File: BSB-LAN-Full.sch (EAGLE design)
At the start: 120 parts, among them IC1 LAN8710A-EZC, IC2 TPS2375D, IC3 TX4138, IC4 SY8089AAAC, IC6 CH340X, Q1 BC847, Q2 BC857, Q3 BC847, Q4 WPM2015-3/TR, Q5 BC847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

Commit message: Add CNMB/3 Footprint and Update Libs
Add footprint for the next size up enclosure.
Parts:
- OPT: device BSB-LAN:JUMPER-2PTH -> BSB-LAN:JUMPER-2-2MM
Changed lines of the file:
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@@
 <attribute name="LCSC_PART" value="C406156"/>
 </part>
-<part name="OPT" library="BSB-LAN" deviceset="JUMPER-2" device="PTH" value="DNI"/>
+<part name="OPT" library="BSB-LAN" deviceset="JUMPER-2" device="-2MM" value="DNI"/>
 <part name="Q5" library="BSB-LAN" deviceset="BC847*" device="" value="BC847">
 <attribute name="LCSC_PART" value="C130417"/>

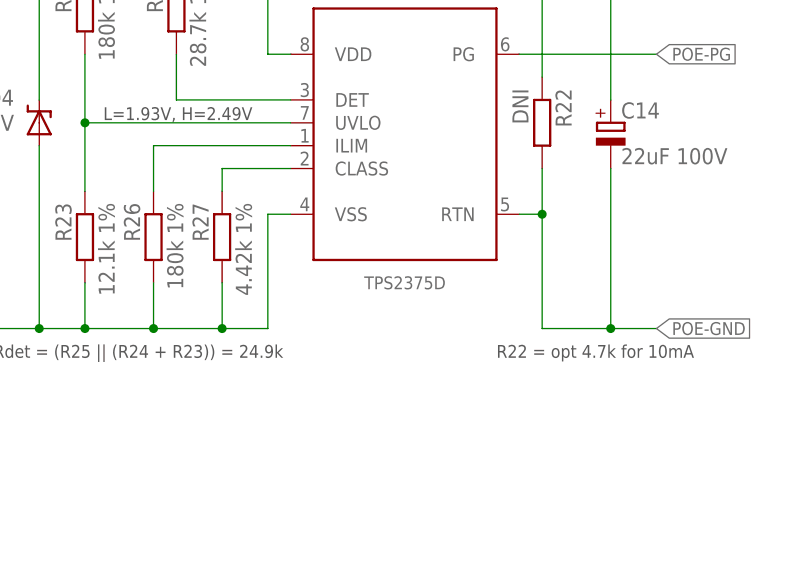
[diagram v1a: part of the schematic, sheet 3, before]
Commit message: Correct PoE IC Part Number
The LCSC_PART selected was the TPS2376DDA but the schematic value was TPS2375D, This actually has a slightly different footprint - the DDA has a thermal pad.

Update to account for the change.
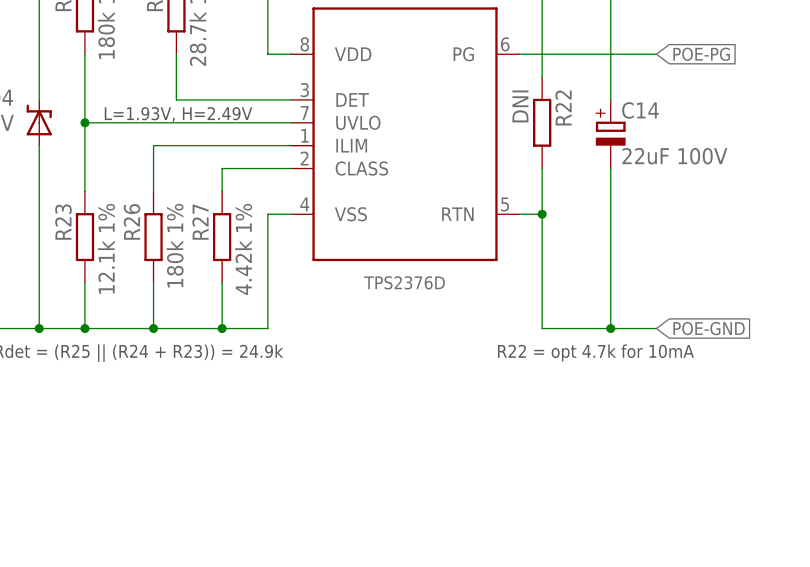
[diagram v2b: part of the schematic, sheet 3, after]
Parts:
- IC2: value TPS2375D -> TPS2376D; device BSB-LAN:TPS2375D -> BSB-LAN:TPS2376D
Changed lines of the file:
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@@
 <grid distance="0.1" unitdist="inch" unit="inch" style="lines" multiple="1" display="no" altdistance="0.01" altunitdist="inch" altunit="inch"/>
 <layers>
-<layer number="1" name="Top" color="4" fill="1" visible="no" active="no"/>
-<layer number="2" name="Route2" color="1" fill="3" visible="no" active="no"/>
-<layer number="3" name="Route3" color="4" fill="3" visible="no" active="no"/>
-<layer number="4" name="Route4" color="1" fill="4" visible="no" active="no"/>
-<layer number="5" name="Route5" color="4" fill="4" visible="no" active="no"/>
-<layer number="6" name="Route6" color="1" fill="8" visible="no" active="no"/>
-<layer number="7" name="Route7" color="4" fill="8" visible="no" active="no"/>
-<layer number="8" name="Route8" color="1" fill="2" visible="no" active="no"/>
-<layer number="9" name="Route9" color="4" fill="2" visible="no" active="no"/>
-<layer number="10" name="Route10" color="1" fill="7" visible="no" active="no"/>
-<layer number="11" name="Route11" color="4" fill="7" visible="no" active="no"/>
-<layer number="12" name="Route12" color="1" fill="5" visible="no" active="no"/>
-<layer number="13" name="Route13" color="4" fill="5" visible="no" active="no"/>
-<layer number="14" name="Route14" color="1" fill="6" visible="no" active="no"/>
-<layer number="15" name="Route15" color="4" fill="6" visible="no" active="no"/>
-<layer number="16" name="Bottom" color="1" fill="1" visible="no" active="no"/>
-<layer number="17" name="Pads" color="2" fill="1" visible="no" active="no"/>
-<layer number="18" name="Vias" color="2" fill="1" visible="no" active="no"/>
-<layer number="19" name="Unrouted" color="6" fill="1" visible="no" active="no"/>
-<layer number="20" name="Dimension" color="15" fill="1" visible="no" active="no"/>
-<layer number="21" name="tPlace" color="7" fill="1" visible="no" active="no"/>
-<layer number="22" name="bPlace" color="7" fill="1" visible="no" active="no"/>
-<layer number="23" name="tOrigins" color="15" fill="1" visible="no" active="no"/>
-<layer number="24" name="bOrigins" color="15" fill="1" visible="no" active="no"/>
-<layer number="25" name="tNames" color="7" fill="1" visible="no" active="no"/>
-<layer number="26" name="bNames" color="7" fill="1" visible="no" active="no"/>
-<layer number="27" name="tValues" color="7" fill="1" visible="no" active="no"/>
-<layer number="28" name="bValues" color="7" fill="1" visible="no" active="no"/>
+<layer number="1" name="Top" color="4" fill="1" visible="yes" active="no"/>
+<layer number="2" name="Route2" color="1" fill="3" visible="yes" active="no"/>
+<layer number="3" name="Route3" color="4" fill="3" visible="yes" active="no"/>
+<layer number="4" name="Route4" color="1" fill="4" visible="yes" active="no"/>
+<layer number="5" name="Route5" color="4" fill="4" visible="yes" active="no"/>
+<layer number="6" name="Route6" color="1" fill="8" visible="yes" active="no"/>
+<layer number="7" name="Route7" color="4" fill="8" visible="yes" active="no"/>
+<layer number="8" name="Route8" color="1" fill="2" visible="yes" active="no"/>
+<layer number="9" name="Route9" color="4" fill="2" visible="yes" active="no"/>
+<layer number="10" name="Route10" color="1" fill="7" visible="yes" active="no"/>
+<layer number="11" name="Route11" color="4" fill="7" visible="yes" active="no"/>
+<layer number="12" name="Route12" color="1" fill="5" visible="yes" active="no"/>
+<layer number="13" name="Route13" color="4" fill="5" visible="yes" active="no"/>
+<layer number="14" name="Route14" color="1" fill="6" visible="yes" active="no"/>
+<layer number="15" name="Route15" color="4" fill="6" visible="yes" active="no"/>
+<layer number="16" name="Bottom" color="1" fill="1" visible="yes" active="no"/>
+<layer number="17" name="Pads" color="2" fill="1" visible="yes" active="no"/>
+<layer number="18" name="Vias" color="2" fill="1" visible="yes" active="no"/>
+<layer number="19" name="Unrouted" color="6" fill="1" visible="yes" active="no"/>
+<layer number="20" name="Dimension" color="15" fill="1" visible="yes" active="no"/>
+<layer number="21" name="tPlace" color="7" fill="1" visible="yes" active="no"/>
+<layer number="22" name="bPlace" color="7" fill="1" visible="yes" active="no"/>
+<layer number="23" name="tOrigins" color="15" fill="1" visible="yes" active="no"/>
+<layer number="24" name="bOrigins" color="15" fill="1" visible="yes" active="no"/>
+<layer number="25" name="tNames" color="7" fill="1" visible="yes" active="no"/>
+<layer number="26" name="bNames" color="7" fill="1" visible="yes" active="no"/>
+<layer number="27" name="tValues" color="7" fill="1" visible="yes" active="no"/>
+<layer number="28" name="bValues" color="7" fill="1" visible="yes" active="no"/>
 <layer number="29" name="tStop" color="7" fill="3" visible="no" active="no"/>
 <layer number="30" name="bStop" color="7" fill="6" visible="no" active="no"/>
@@
 <layer number="35" name="tGlue" color="7" fill="4" visible="no" active="no"/>
 <layer number="36" name="bGlue" color="7" fill="5" visible="no" active="no"/>
-<layer number="37" name="tTest" color="7" fill="1" visible="no" active="no"/>
-<layer number="38" name="bTest" color="7" fill="1" visible="no" active="no"/>
+<layer number="37" name="tTest" color="7" fill="1" visible="yes" active="no"/>
+<layer number="38" name="bTest" color="7" fill="1" visible="yes" active="no"/>
 <layer number="39" name="tKeepout" color="4" fill="11" visible="no" active="no"/>
 <layer number="40" name="bKeepout" color="1" fill="11" visible="no" active="no"/>
@@
 <layer number="44" name="Drills" color="7" fill="1" visible="no" active="no"/>
 <layer number="45" name="Holes" color="7" fill="1" visible="no" active="no"/>
-<layer number="46" name="Milling" color="3" fill="1" visible="no" active="no"/>
-<layer number="47" name="Measures" color="7" fill="1" visible="no" active="no"/>
-<layer number="48" name="Document" color="7" fill="1" visible="no" active="no"/>
-<layer number="49" name="Reference" color="7" fill="1" visible="no" active="no"/>
-<layer number="50" name="dxf" color="7" fill="1" visible="no" active="no"/>
-<layer number="51" name="tDocu" color="7" fill="1" visible="no" active="no"/>
-<layer number="52" name="bDocu" color="7" fill="1" visible="no" active="no"/>
-<layer number="53" name="tGND_GNDA" color="7" fill="9" visible="no" active="no"/>
-<layer number="54" name="bGND_GNDA" color="1" fill="9" visible="no" active="no"/>
-<layer number="56" name="wert" color="7" fill="1" visible="no" active="no"/>
-<layer number="57" name="tCAD" color="7" fill="1" visible="no" active="no"/>
-<layer number="58" name="bCAD" color="7" fill="1" visible="no" active="no"/>
-<layer number="59" name="tCarbon" color="7" fill="1" visible="no" active="no"/>
-<layer number="60" name="bCarbon" color="7" fill="1" visible="no" active="no"/>
+<layer number="46" name="Milling" color="3" fill="1" visible="yes" active="no"/>
+<layer number="47" name="Measures" color="7" fill="1" visible="yes" active="no"/>
+<layer number="48" name="Document" color="7" fill="1" visible="yes" active="no"/>
+<layer number="49" name="Reference" color="7" fill="1" visible="yes" active="no"/>
+<layer number="50" name="dxf" color="7" fill="1" visible="yes" active="no"/>
+<layer number="51" name="tDocu" color="7" fill="1" visible="yes" active="no"/>
+<layer number="52" name="bDocu" color="7" fill="1" visible="yes" active="no"/>
+<layer number="53" name="tGND_GNDA" color="7" fill="9" visible="yes" active="no"/>
+<layer number="54" name="bGND_GNDA" color="1" fill="9" visible="yes" active="no"/>
+<layer number="56" name="wert" color="7" fill="1" visible="yes" active="no"/>
+<layer number="57" name="tCAD" color="7" fill="1" visible="yes" active="no"/>
+<layer number="58" name="bCAD" color="7" fill="1" visible="yes" active="no"/>
+<layer number="59" name="tCarbon" color="7" fill="1" visible="yes" active="no"/>
+<layer number="60" name="bCarbon" color="7" fill="1" visible="yes" active="no"/>
 <layer number="88" name="SimResults" color="9" fill="1" visible="yes" active="yes"/>
 <layer number="89" name="SimProbes" color="9" fill="1" visible="yes" active="yes"/>
@@
 <attribute name="LCSC_PART" value="C113803"/>
 </part>
-<part name="IC2" library="BSB-LAN" deviceset="TPS2375" device="D"/>
+<part name="IC2" library="BSB-LAN" deviceset="TPS237*" device="D" technology="6"/>
 <part name="D4" library="BSB-LAN" deviceset="TVS-UNI" device="SMA" value="58V">
 <attribute name="LCSC_PART" value="C151246"/>

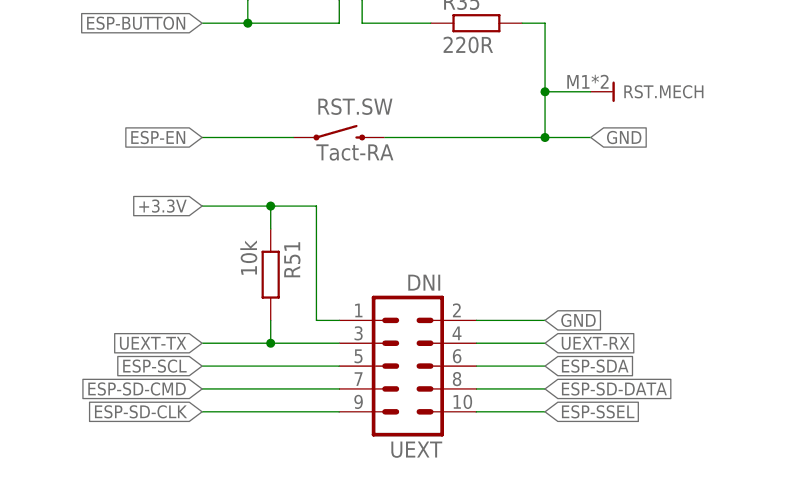
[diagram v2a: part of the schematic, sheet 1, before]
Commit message: Correct Component Rotation Values in JLC CPL
Add rotation correction factors to parts which import in the wrong orientation.
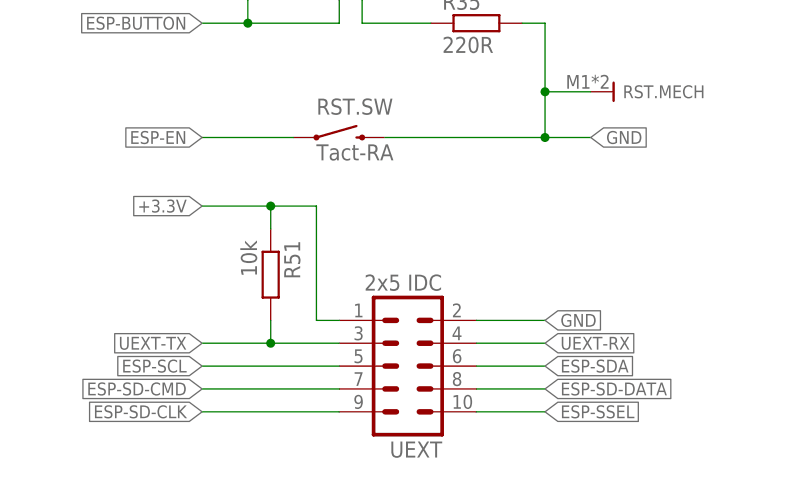
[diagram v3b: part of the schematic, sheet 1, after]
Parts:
- UEXT: value DNI -> 2x5 IDC
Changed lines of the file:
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@@
 <grid distance="0.1" unitdist="inch" unit="inch" style="lines" multiple="1" display="no" altdistance="0.01" altunitdist="inch" altunit="inch"/>
 <layers>
-<layer number="1" name="Top" color="4" fill="1" visible="yes" active="no"/>
-<layer number="2" name="Route2" color="1" fill="3" visible="yes" active="no"/>
-<layer number="3" name="Route3" color="4" fill="3" visible="yes" active="no"/>
-<layer number="4" name="Route4" color="1" fill="4" visible="yes" active="no"/>
-<layer number="5" name="Route5" color="4" fill="4" visible="yes" active="no"/>
-<layer number="6" name="Route6" color="1" fill="8" visible="yes" active="no"/>
-<layer number="7" name="Route7" color="4" fill="8" visible="yes" active="no"/>
-<layer number="8" name="Route8" color="1" fill="2" visible="yes" active="no"/>
-<layer number="9" name="Route9" color="4" fill="2" visible="yes" active="no"/>
-<layer number="10" name="Route10" color="1" fill="7" visible="yes" active="no"/>
-<layer number="11" name="Route11" color="4" fill="7" visible="yes" active="no"/>
-<layer number="12" name="Route12" color="1" fill="5" visible="yes" active="no"/>
-<layer number="13" name="Route13" color="4" fill="5" visible="yes" active="no"/>
-<layer number="14" name="Route14" color="1" fill="6" visible="yes" active="no"/>
-<layer number="15" name="Route15" color="4" fill="6" visible="yes" active="no"/>
-<layer number="16" name="Bottom" color="1" fill="1" visible="yes" active="no"/>
-<layer number="17" name="Pads" color="2" fill="1" visible="yes" active="no"/>
-<layer number="18" name="Vias" color="2" fill="1" visible="yes" active="no"/>
-<layer number="19" name="Unrouted" color="6" fill="1" visible="yes" active="no"/>
-<layer number="20" name="Dimension" color="15" fill="1" visible="yes" active="no"/>
-<layer number="21" name="tPlace" color="7" fill="1" visible="yes" active="no"/>
-<layer number="22" name="bPlace" color="7" fill="1" visible="yes" active="no"/>
-<layer number="23" name="tOrigins" color="15" fill="1" visible="yes" active="no"/>
-<layer number="24" name="bOrigins" color="15" fill="1" visible="yes" active="no"/>
-<layer number="25" name="tNames" color="7" fill="1" visible="yes" active="no"/>
-<layer number="26" name="bNames" color="7" fill="1" visible="yes" active="no"/>
-<layer number="27" name="tValues" color="7" fill="1" visible="yes" active="no"/>
-<layer number="28" name="bValues" color="7" fill="1" visible="yes" active="no"/>
+<layer number="1" name="Top" color="4" fill="1" visible="no" active="no"/>
+<layer number="2" name="Route2" color="1" fill="3" visible="no" active="no"/>
+<layer number="3" name="Route3" color="4" fill="3" visible="no" active="no"/>
+<layer number="4" name="Route4" color="1" fill="4" visible="no" active="no"/>
+<layer number="5" name="Route5" color="4" fill="4" visible="no" active="no"/>
+<layer number="6" name="Route6" color="1" fill="8" visible="no" active="no"/>
+<layer number="7" name="Route7" color="4" fill="8" visible="no" active="no"/>
+<layer number="8" name="Route8" color="1" fill="2" visible="no" active="no"/>
+<layer number="9" name="Route9" color="4" fill="2" visible="no" active="no"/>
+<layer number="10" name="Route10" color="1" fill="7" visible="no" active="no"/>
+<layer number="11" name="Route11" color="4" fill="7" visible="no" active="no"/>
+<layer number="12" name="Route12" color="1" fill="5" visible="no" active="no"/>
+<layer number="13" name="Route13" color="4" fill="5" visible="no" active="no"/>
+<layer number="14" name="Route14" color="1" fill="6" visible="no" active="no"/>
+<layer number="15" name="Route15" color="4" fill="6" visible="no" active="no"/>
+<layer number="16" name="Bottom" color="1" fill="1" visible="no" active="no"/>
+<layer number="17" name="Pads" color="2" fill="1" visible="no" active="no"/>
+<layer number="18" name="Vias" color="2" fill="1" visible="no" active="no"/>
+<layer number="19" name="Unrouted" color="6" fill="1" visible="no" active="no"/>
+<layer number="20" name="Dimension" color="15" fill="1" visible="no" active="no"/>
+<layer number="21" name="tPlace" color="7" fill="1" visible="no" active="no"/>
+<layer number="22" name="bPlace" color="7" fill="1" visible="no" active="no"/>
+<layer number="23" name="tOrigins" color="15" fill="1" visible="no" active="no"/>
+<layer number="24" name="bOrigins" color="15" fill="1" visible="no" active="no"/>
+<layer number="25" name="tNames" color="7" fill="1" visible="no" active="no"/>
+<layer number="26" name="bNames" color="7" fill="1" visible="no" active="no"/>
+<layer number="27" name="tValues" color="7" fill="1" visible="no" active="no"/>
+<layer number="28" name="bValues" color="7" fill="1" visible="no" active="no"/>
 <layer number="29" name="tStop" color="7" fill="3" visible="no" active="no"/>
 <layer number="30" name="bStop" color="7" fill="6" visible="no" active="no"/>
@@
 <layer number="35" name="tGlue" color="7" fill="4" visible="no" active="no"/>
 <layer number="36" name="bGlue" color="7" fill="5" visible="no" active="no"/>
-<layer number="37" name="tTest" color="7" fill="1" visible="yes" active="no"/>
-<layer number="38" name="bTest" color="7" fill="1" visible="yes" active="no"/>
+<layer number="37" name="tTest" color="7" fill="1" visible="no" active="no"/>
+<layer number="38" name="bTest" color="7" fill="1" visible="no" active="no"/>
 <layer number="39" name="tKeepout" color="4" fill="11" visible="no" active="no"/>
 <layer number="40" name="bKeepout" color="1" fill="11" visible="no" active="no"/>
@@
 <layer number="44" name="Drills" color="7" fill="1" visible="no" active="no"/>
 <layer number="45" name="Holes" color="7" fill="1" visible="no" active="no"/>
-<layer number="46" name="Milling" color="3" fill="1" visible="yes" active="no"/>
-<layer number="47" name="Measures" color="7" fill="1" visible="yes" active="no"/>
-<layer number="48" name="Document" color="7" fill="1" visible="yes" active="no"/>
-<layer number="49" name="Reference" color="7" fill="1" visible="yes" active="no"/>
-<layer number="50" name="dxf" color="7" fill="1" visible="yes" active="no"/>
-<layer number="51" name="tDocu" color="7" fill="1" visible="yes" active="no"/>
-<layer number="52" name="bDocu" color="7" fill="1" visible="yes" active="no"/>
-<layer number="53" name="tGND_GNDA" color="7" fill="9" visible="yes" active="no"/>
-<layer number="54" name="bGND_GNDA" color="1" fill="9" visible="yes" active="no"/>
-<layer number="56" name="wert" color="7" fill="1" visible="yes" active="no"/>
-<layer number="57" name="tCAD" color="7" fill="1" visible="yes" active="no"/>
-<layer number="58" name="bCAD" color="7" fill="1" visible="yes" active="no"/>
-<layer number="59" name="tCarbon" color="7" fill="1" visible="yes" active="no"/>
-<layer number="60" name="bCarbon" color="7" fill="1" visible="yes" active="no"/>
+<layer number="46" name="Milling" color="3" fill="1" visible="no" active="no"/>
+<layer number="47" name="Measures" color="7" fill="1" visible="no" active="no"/>
+<layer number="48" name="Document" color="7" fill="1" visible="no" active="no"/>
+<layer number="49" name="Reference" color="7" fill="1" visible="no" active="no"/>
+<layer number="50" name="dxf" color="7" fill="1" visible="no" active="no"/>
+<layer number="51" name="tDocu" color="7" fill="1" visible="no" active="no"/>
+<layer number="52" name="bDocu" color="7" fill="1" visible="no" active="no"/>
+<layer number="53" name="tGND_GNDA" color="7" fill="9" visible="no" active="no"/>
+<layer number="54" name="bGND_GNDA" color="1" fill="9" visible="no" active="no"/>
+<layer number="56" name="wert" color="7" fill="1" visible="no" active="no"/>
+<layer number="57" name="tCAD" color="7" fill="1" visible="no" active="no"/>
+<layer number="58" name="bCAD" color="7" fill="1" visible="no" active="no"/>
+<layer number="59" name="tCarbon" color="7" fill="1" visible="no" active="no"/>
+<layer number="60" name="bCarbon" color="7" fill="1" visible="no" active="no"/>
 <layer number="88" name="SimResults" color="9" fill="1" visible="yes" active="yes"/>
 <layer number="89" name="SimProbes" color="9" fill="1" visible="yes" active="yes"/>
@@
 <attribute name="LCSC_PART" value="C426782"/>
 </part>
-<part name="UEXT" library="BSB-LAN" deviceset="ML10" device="" value="DNI"/>
+<part name="UEXT" library="BSB-LAN" deviceset="ML10" device="" value="2x5 IDC"/>
 <part name="ACT" library="BSB-LAN" deviceset="LED" device="CHIPLED_0603" value="red">
 <attribute name="LCSC_PART" value="C2286"/>
